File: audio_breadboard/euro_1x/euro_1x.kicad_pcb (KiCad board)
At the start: 2 copper layers, 182.9 x 87.6 mm, 32 parts, among them J1 EURO POWER, J10 IN, J11 IN, J12 OUT, J13 OUT, J14 AUX1, J15 AUX2, J16 Jumper, J17 Jumper, J18 GND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

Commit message: Complete Euro 2x
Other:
- board text added: "Euro 1x"
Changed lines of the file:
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@@
     (effects (font (size 1 1) (thickness 0.15)) (justify right))
+  )
+  (gr_text "Euro 1x" (at 152.4 45.72) (layer "Cmts.User")
+    (effects (font (size 5 5) (thickness 0.75)))
   )
   (segment (start 203.835 80.01) (end 168.907208 80.01) (width 1) (layer "F.Cu") (net 1))

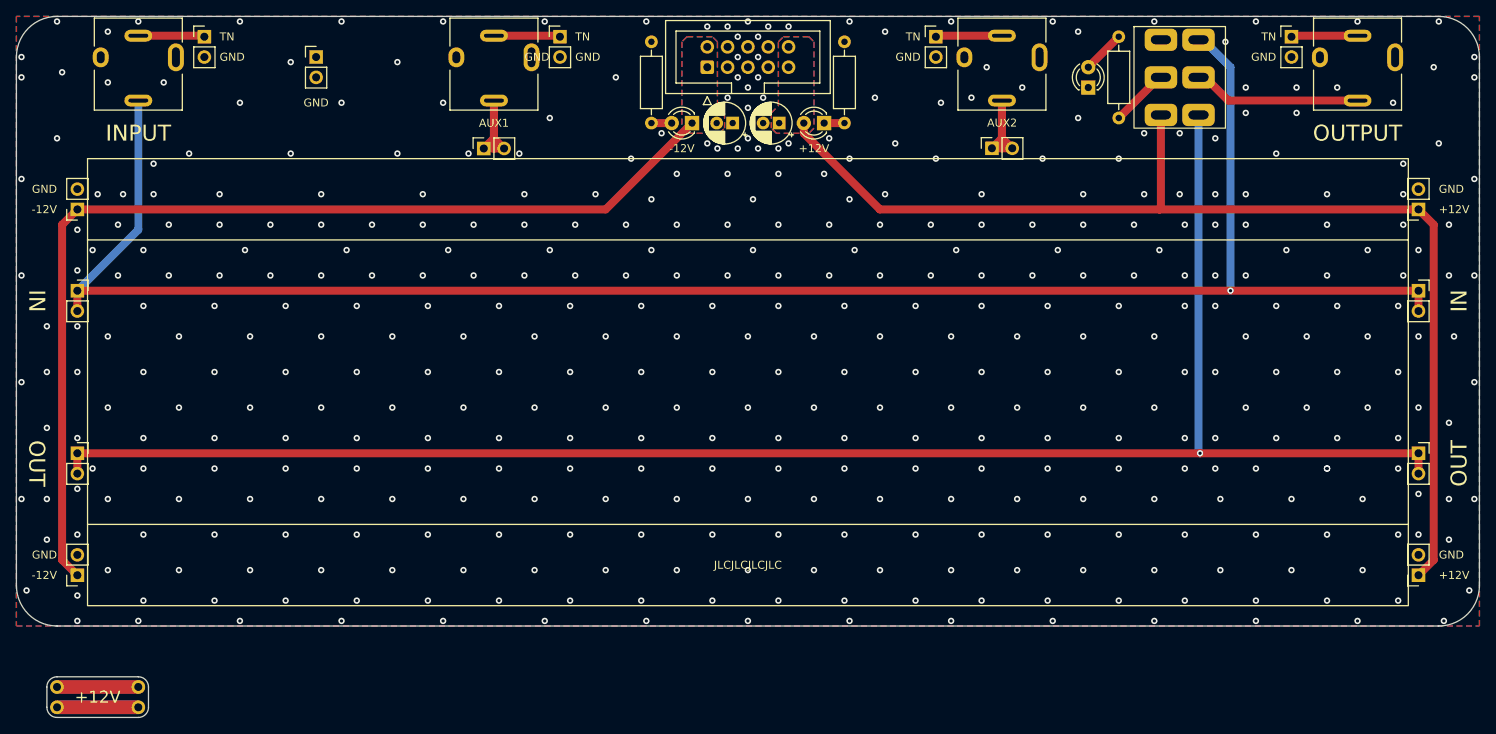
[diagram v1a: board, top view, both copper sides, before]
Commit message: fix breadboard footprint
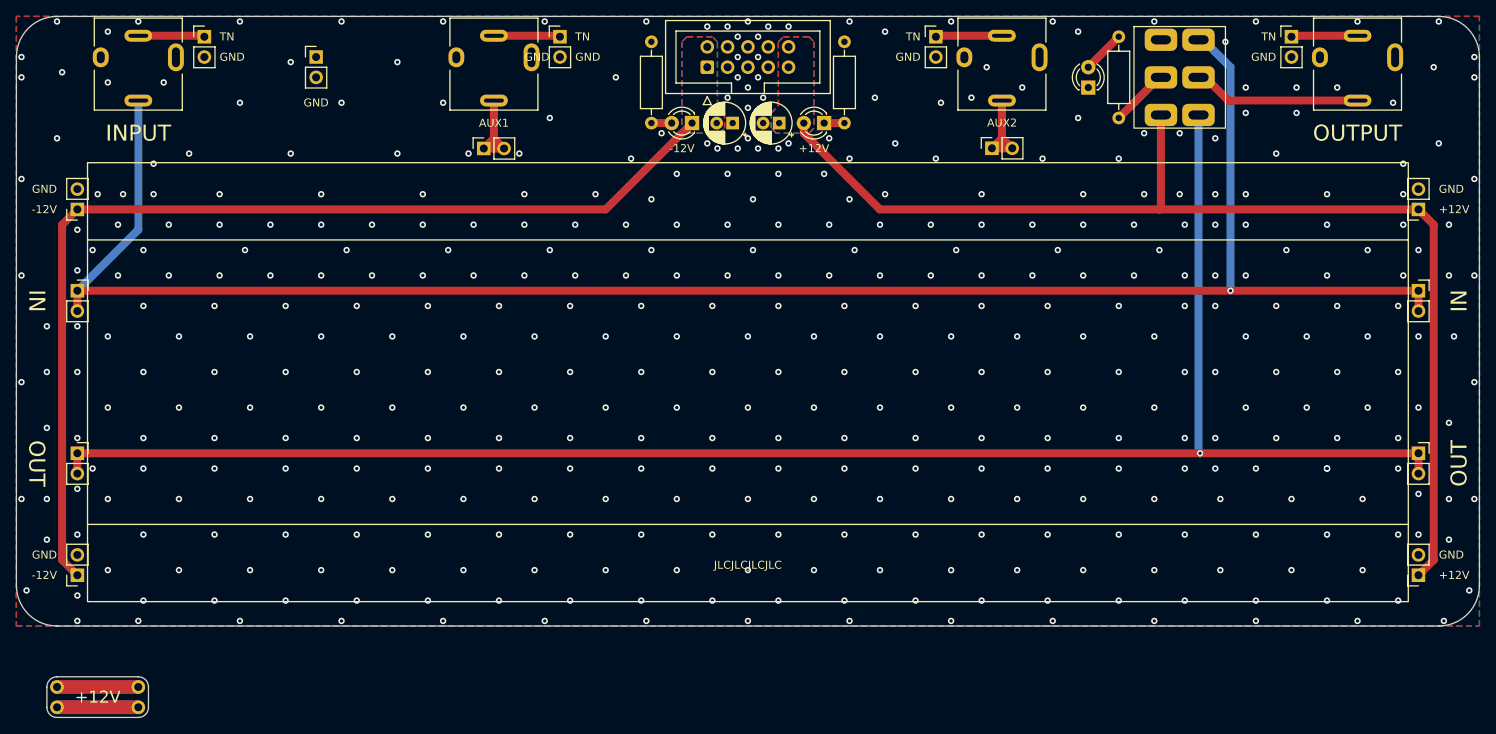
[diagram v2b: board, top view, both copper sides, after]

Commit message: Fix euro1x with latest breadboard footprint
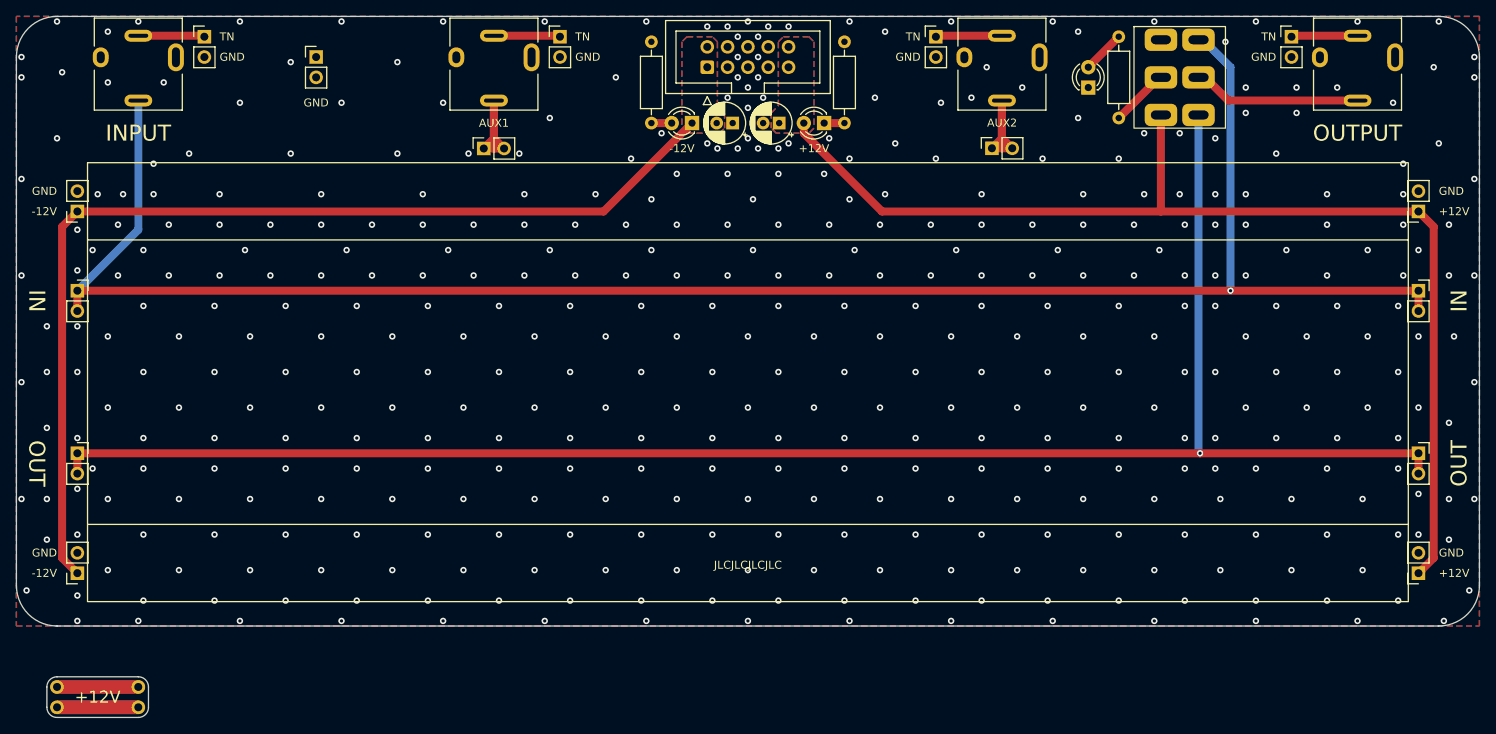
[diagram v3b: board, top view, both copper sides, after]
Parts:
- moved J7 0.25 mm to (236.2, 125.5)
- moved J9 0.25 mm to (68.6, 125.5)
- moved J6 0.25 mm to (236.2, 80.3)
- moved J8 0.25 mm to (68.6, 80.3)
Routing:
- net GND: vias 423 -> 422
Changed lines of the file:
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@@
   (net 19 "Net-(J16-Pin_2)")
   (footprint "Connector_PinSocket_2.54mm:PinSocket_1x02_P2.54mm_Vertical" (layer "F.Cu")
-    (at 68.58 125.73 180)
+    (at 68.58 125.476 180)
     (descr "Through hole straight socket strip, 1x02, 2.54mm pitch, single row (from Kicad 4.0.7), script generated")
     (tags "Through hole socket strip THT 1x02 2.54mm single row")
@@
   )
   (footprint "Connector_PinSocket_2.54mm:PinSocket_1x02_P2.54mm_Vertical" (layer "F.Cu")
-    (at 236.22 125.73 180)
+    (at 236.22 125.476 180)
     (descr "Through hole straight socket strip, 1x02, 2.54mm pitch, single row (from Kicad 4.0.7), script generated")
     (tags "Through hole socket strip THT 1x02 2.54mm single row")
@@
   )
   (footprint "Connector_PinSocket_2.54mm:PinSocket_1x02_P2.54mm_Vertical" (layer "F.Cu")
-    (at 68.58 80.01 180)
+    (at 68.58 80.264 180)
     (descr "Through hole straight socket strip, 1x02, 2.54mm pitch, single row (from Kicad 4.0.7), script generated")
     (tags "Through hole socket strip THT 1x02 2.54mm single row")
@@
   )
   (footprint "Connector_PinSocket_2.54mm:PinSocket_1x02_P2.54mm_Vertical" (layer "F.Cu")
-    (at 236.22 80.01 180)
+    (at 236.22 80.264 180)
     (descr "Through hole straight socket strip, 1x02, 2.54mm pitch, single row (from Kicad 4.0.7), script generated")
     (tags "Through hole socket strip THT 1x02 2.54mm single row")
@@
     (effects (font (size 1 1) (thickness 0.15)) (justify right))
   )
-  (gr_text "GND" (at 66.04 77.47) (layer "F.SilkS" knockout)
+  (gr_text "GND" (at 66.04 77.724) (layer "F.SilkS" knockout)
     (effects (font (size 1 1) (thickness 0.15)) (justify right))
   )
@@
     (effects (font (size 1 1) (thickness 0.15)) (justify right))
   )
-  (gr_text "GND" (at 238.76 77.47) (layer "F.SilkS" knockout)
+  (gr_text "GND" (at 238.76 77.724) (layer "F.SilkS" knockout)
     (effects (font (size 1 1) (thickness 0.15)) (justify left))
   )
@@
     (effects (font (size 1 1) (thickness 0.15)) (justify left))
   )
-  (gr_text "GND" (at 124.46 60.96) (layer "F.SilkS")
-    (effects (font (size 1 1) (thickness 0.15)) (justify left))
-  )
-  (gr_text "GND" (at 238.76 123.19) (layer "F.SilkS" knockout)
+  (gr_text "GND" (at 238.76 122.936) (layer "F.SilkS" knockout)
     (effects (font (size 1 1) (thickness 0.15)) (justify left))
   )
@@
     (effects (font (size 1 1) (thickness 0.15)) (justify left))
   )
-  (gr_text "GND" (at 66.04 123.19) (layer "F.SilkS" knockout)
+  (gr_text "GND" (at 66.04 122.936) (layer "F.SilkS" knockout)
     (effects (font (size 1 1) (thickness 0.15)) (justify right))
   )
@@
     (effects (font (size 5 5) (thickness 0.75)))
   )
-  (segment (start 203.835 80.01) (end 168.907208 80.01) (width 1) (layer "F.Cu") (net 1))
-  (segment (start 204.0255 79.8195) (end 203.835 80.01) (width 1) (layer "F.Cu") (net 1))
-  (segment (start 236.22 80.01) (end 203.835 80.01) (width 1) (layer "F.Cu") (net 1))
-  (segment (start 238.125 81.915) (end 238.125 123.825) (width 1) (layer "F.Cu") (net 1))
-  (segment (start 236.22 80.01) (end 238.125 81.915) (width 1) (layer "F.Cu") (net 1))
-  (segment (start 168.907208 80.01) (end 159.385 70.487792) (width 1) (layer "F.Cu") (net 1))
-  (segment (start 204.0255 68.199) (end 204.0255 79.8195) (width 1) (layer "F.Cu") (net 1))
+  (segment (start 238.125 82.169) (end 236.22 80.264) (width 1) (layer "F.Cu") (net 1))
   (segment (start 159.385 70.487792) (end 159.385 69.215) (width 1) (layer "F.Cu") (net 1))
-  (segment (start 238.125 123.825) (end 236.22 125.73) (width 1) (layer "F.Cu") (net 1))
+  (segment (start 169.161208 80.264) (end 159.385 70.487792) (width 1) (layer "F.Cu") (net 1))
+  (segment (start 236.22 125.476) (end 238.125 123.571) (width 1) (layer "F.Cu") (net 1))
+  (segment (start 238.125 123.571) (end 238.125 82.169) (width 1) (layer "F.Cu") (net 1))
+  (segment (start 236.22 80.264) (end 169.161208 80.264) (width 1) (layer "F.Cu") (net 1))
+  (segment (start 204.0255 68.199) (end 204.0255 80.264) (width 1) (layer "F.Cu") (net 1))
   (via (at 164.465 112.395) (size 0.8) (drill 0.4) (layers "F.Cu" "B.Cu") (free) (net 2))
   (via (at 143.51 116.205) (size 0.8) (drill 0.4) (layers "F.Cu" "B.Cu") (free) (net 2))
@@
   (via (at 168.91 104.775) (size 0.8) (drill 0.4) (layers "F.Cu" "B.Cu") (free) (net 2))
   (via (at 134.62 95.885) (size 0.8) (drill 0.4) (layers "F.Cu" "B.Cu") (free) (net 2))
-  (via (at 224.79 112.395) (size 0.8) (drill 0.4) (layers "F.Cu" "B.Cu") (free) (net 2))
   (via (at 240.665 95.885) (size 0.8) (drill 0.4) (layers "F.Cu" "B.Cu") (free) (net 2))
   (via (at 112.395 128.905) (size 0.8) (drill 0.4) (layers "F.Cu" "B.Cu") (free) (net 2))
@@
   (via (at 189.865 92.075) (size 0.8) (drill 0.4) (layers "F.Cu" "B.Cu") (free) (net 2))
   (via (at 130.81 88.265) (size 0.8) (drill 0.4) (layers "F.Cu" "B.Cu") (free) (net 2))
-  (segment (start 66.675 81.915) (end 66.675 123.825) (width 1) (layer "F.Cu") (net 3))
-  (segment (start 66.675 123.825) (end 68.58 125.73) (width 1) (layer "F.Cu") (net 3))
-  (segment (start 68.58 80.01) (end 134.62 80.01) (width 1) (layer "F.Cu") (net 3))
-  (segment (start 68.58 80.01) (end 66.675 81.915) (width 1) (layer "F.Cu") (net 3))
-  (segment (start 134.62 80.01) (end 145.415 69.215) (width 1) (layer "F.Cu") (net 3))
+  (segment (start 66.675 82.169) (end 66.675 123.571) (width 1) (layer "F.Cu") (net 3))
+  (segment (start 66.675 123.571) (end 68.58 125.476) (width 1) (layer "F.Cu") (net 3))
+  (segment (start 134.366 80.264) (end 68.58 80.264) (width 1) (layer "F.Cu") (net 3))
+  (segment (start 145.415 69.215) (end 134.366 80.264) (width 1) (layer "F.Cu") (net 3))
+  (segment (start 68.58 80.264) (end 66.675 82.169) (width 1) (layer "F.Cu") (net 3))
   (segment (start 161.925 69.215) (end 164.465 69.215) (width 1) (layer "F.Cu") (net 4))
   (segment (start 84.33 58.295) (end 84.455 58.42) (width 1) (layer "F.Cu") (net 5))
